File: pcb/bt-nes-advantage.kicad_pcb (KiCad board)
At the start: 2 copper layers, 78 x 36.5 mm, 28 parts, among them J1 PJ-043-SMT-TR, J2 Conn_01x08_Socket, J3 3.7V Lithium Battery, U1 TP4057, U2 TPS613222ADBV, U3 ESP32-C3_SUPERMINI_TH

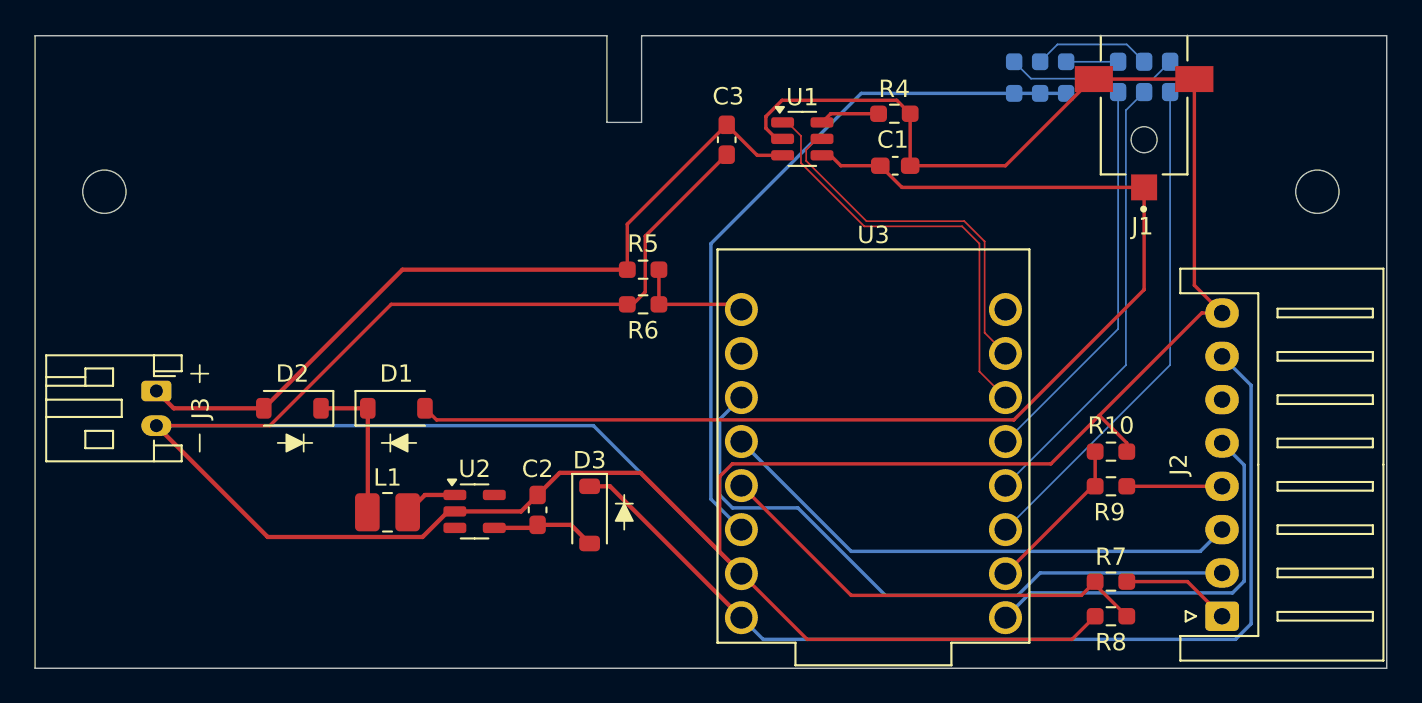
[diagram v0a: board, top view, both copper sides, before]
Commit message: Updated PCB shape to clear the back panel wedge on some versions of the NES Advantage,
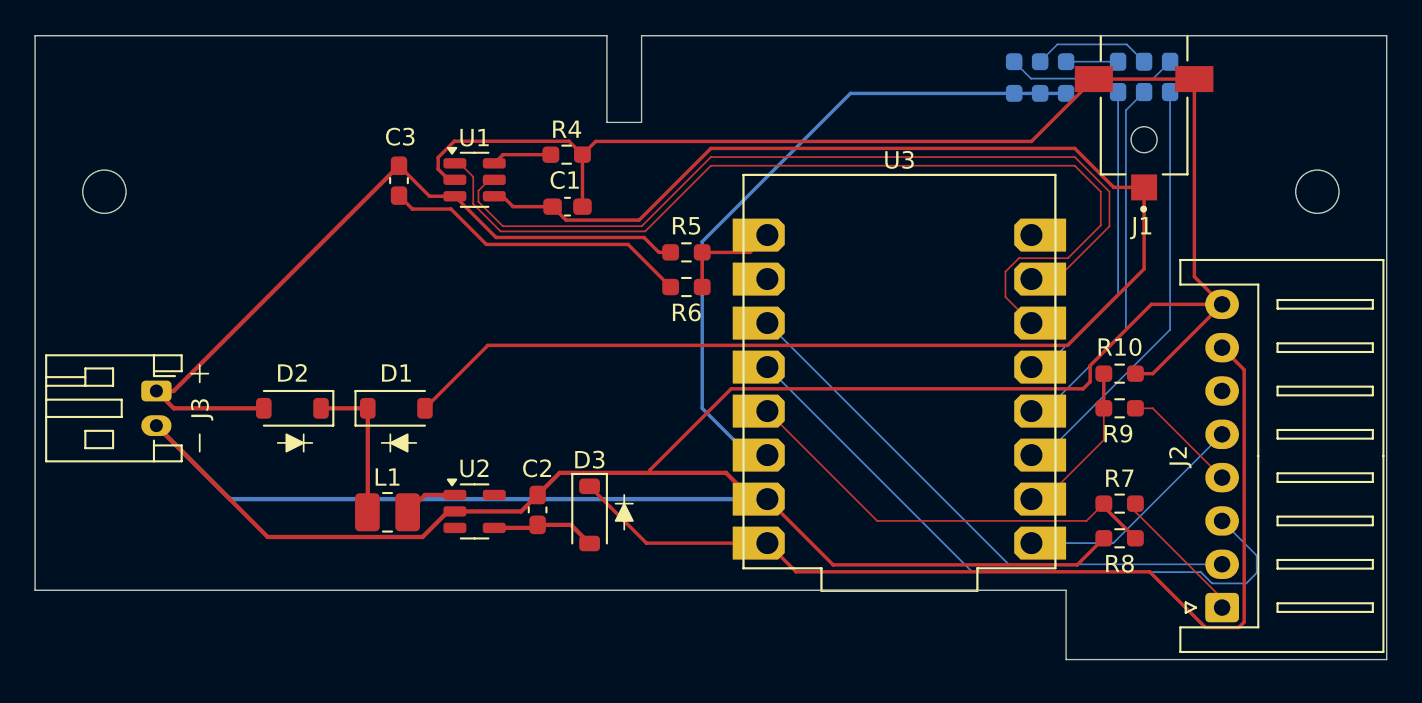
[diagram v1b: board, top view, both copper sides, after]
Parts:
- U3: footprint My_Library:MODULE_ESP32-C3_SUPERMINI -> My_Library:MODULE_ESP32-C3_SUPERMINI_SMD
- moved U1 19.1 mm to (125.4, 108.3)
- moved C1 19.1 mm to (130.7, 109.9)
- moved C3 19.1 mm to (121.0, 108.4)
- moved R4 19.1 mm to (130.7, 106.9)
- moved U3 4.55 mm to (149.9, 119.4)
- moved R10 4.53 mm to (162.6, 119.5)
- moved R7 4.53 mm to (162.6, 127.0)
- moved R8 4.53 mm to (162.6, 129.0)
- moved R9 4.53 mm to (162.6, 121.5)
- moved R5 2.69 mm to (137.6, 112.5)
- moved R6 2.69 mm to (137.6, 114.5)
- moved J2 0.50 mm to (168.5, 133.0)
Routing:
- net BATT_CHRG: track 24.7 -> 54.1 mm
- net BATT_STDBY: track 21.0 -> 49.1 mm
- net VBUS_5V: track 70.1 -> 90.3 mm
- net CLOCK_1: track 23.2 -> 13.6 mm
- net CLOCK_0: track 30.9 -> 37.5 mm
- net LATCH: track 38.1 -> 32.0 mm
- net LED3: track 22.9 -> 18.4 mm
- net LED1: track 29.2 -> 24.7 mm
- net LED2: track 26.0 -> 21.6 mm
- net GND: track 229.8 -> 225.6 mm
- net VDD_3V: track 41.3 -> 39.0 mm
- net VBAT: track 45.6 -> 43.7 mm
- net DATA_0_5V: track 6.33 -> 8.07 mm
- net DATA_1_5V: track 5.50 -> 6.66 mm
- net DATA_0: track 26.1 -> 25.2 mm
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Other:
- board size 78 x 36.5 mm -> 78 x 36 mm
- board text added: "Bluetooth NES Advantage 1.1"
- board text removed: "Bluetooth NES Advantage 1.0"

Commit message: Added missing ground trace for battery voltage detection.
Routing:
- net GND: track 225.6 -> 248.5 mm
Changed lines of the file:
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@@
+	)
+	(segment
+		(start 121 115.05011)
+		(end 113.55011 122.5)
+		(width 0.2)
+		(layer "F.Cu")
+		(net 1)
 	)
 	(segment
@@
 		(end 139.870466 125.224)
 		(width 0.25)
+		(layer "F.Cu")
+		(net 1)
+	)
+	(segment
+		(start 121 109.225)
+		(end 121 115.05011)
+		(width 0.2)
 		(layer "F.Cu")
 		(net 1)
@@
 		(width 0.2)
 		(layer "F.Cu")
+		(net 1)
+	)
+	(segment
+		(start 113.55011 122.5)
+		(end 107 122.5)
+		(width 0.2)
+		(layer "F.Cu")

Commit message: Updated board revision.
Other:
- board text added: "Bluetooth NES Advantage 1.2"
- board text removed: "Bluetooth NES Advantage 1.1"
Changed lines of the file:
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@@
 		)
 	)
-	(gr_text "Bluetooth NES Advantage 1.1"
+	(gr_text "Bluetooth NES Advantage 1.2"
 		(at 137.5 117.5 0)
 		(layer "B.SilkS")
@@
 			(justify left bottom mirror)
 		)
-		(render_cache "Bluetooth NES Advantage 1.1" 0
+		(render_cache "Bluetooth NES Advantage 1.2" 0
 			(polygon
 				(pts
@@
 			(polygon
 				(pts
-					(xy 102.530286 117.16) (xy 102.530286 116.885593) (xy 102.053401 116.885593) (xy 102.053401 116.336779)
-					(xy 102.062745 116.274284) (xy 102.087533 116.23374) (xy 102.127765 116.208865) (xy 102.189567 116.199515)
-					(xy 102.257711 116.199515) (xy 102.257711 115.925108) (xy 101.779972 115.925108) (xy 101.779972 116.885593)
-					(xy 101.30321 116.885593) (xy 101.30321 117.16)
-				)
-			)
+					(xy 102.530286 115.925108) (xy 101.712316 115.925108) (xy 101.577752 115.937588) (xy 101.477405 115.971199)
+					(xy 101.403176 116.022726) (xy 101.349816 116.092648) (xy 101.315717 116.185033) (xy 101.30321 116.306859)
+					(xy 101.315624 116.426615) (xy 101.349511 116.517579) (xy 101.402647 116.586578) (xy 101.476742 116.637546)
+					(xy 101.577124 116.670856) (xy 101.71195 116.683237) (xy 102.120568 116.683237) (xy 102.182651 116.692501)
+					(xy 102.222905 116.717063) (xy 102.247584 116.7569) (xy 102.256856 116.81806) (xy 102.256856 116.885593)
+					(xy 101.30321 116.885593) (xy 101.30321 117.16) (xy 102.530286 117.16) (xy 102.530286 116.818548)
+					(xy 102.517345 116.685714) (xy 102.482289 116.58586) (xy 102.42802 116.51118) (xy 102.353494 116.456846)
+					(xy 102.253924 116.421773) (xy 102.121545 116.408831) (xy 101.712927 116.408831) (xy 101.648008 116.400735)
+					(xy 101.607962 116.380102) (xy 101.584918 116.348642) (xy 101.576639 116.302829) (xy 101.584815 116.258417)
+					(xy 101.607688 116.227741) (xy 101.647711 116.207491) (xy 101.712927 116.199515) (xy 102.530286 116.199515)
+				)
+			)
